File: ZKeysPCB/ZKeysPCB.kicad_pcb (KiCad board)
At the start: 2 copper layers, 73.7 x 50.8 mm, 15 parts, among them SW1 SW_Push, SW2 SW_Push, SW3 SW_Push, SW4 SW_Push, SW5 SW_Push, SW6 SW_Push, U1 Teensy-LC

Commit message: updated PCB drawing
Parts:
- removed the REF** at (87.6, 90.2)
- removed the REF** at (87.6, 132.1)
- removed the REF** at (153.7, 132.1)
- added REF**: MountingHole_3.2mm_M3, MountingHole:MountingHole_3.2mm_M3, F.Cu at (69.8, 127.0)
- added REF**: MountingHole_3.2mm_M3, MountingHole:MountingHole_3.2mm_M3, F.Cu at (69.8, 94.0)
- added REF**: MountingHole_3.2mm_M3, MountingHole:MountingHole_3.2mm_M3, F.Cu at (153.0, 127.0)
- U1: moved to F.Cu
- moved R2 68.9 mm to (68.6, 109.9), turned to 90 degrees
- moved KEY 59.4 mm to (71.8, 119.4)
- moved PWR 43.2 mm to (71.8, 114.3), turned to 180 degrees
- moved R1 42.1 mm to (71.8, 109.9), turned to 90 degrees
- moved U1 4.58 mm to (82.5, 106.7)
- moved REF** 3.24 mm to (153.0, 93.3)
- moved SW4 2.84 mm to (104.1, 115.6)
- moved SW1 2.54 mm to (104.1, 95.2)
- moved SW5 1.80 mm to (124.5, 115.6)
- moved SW6 1.27 mm to (144.8, 115.6)
- moved SW2 1.27 mm to (124.5, 95.2)
- renumbered D2 to KEY, D1 to PWR
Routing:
- net BTN_INC: track 49.4 -> 90.5 mm
- net BTN_DEC: track 28.2 -> 56.0 mm
- net Net-(D1-Pad2): track 42.5 -> 16.0 mm
- net GND: track 25.6 -> 0.00 mm
- net Net-(D2-Pad2): track 33.3 -> 8.04 mm
- net BTN_MUTE: track 10.7 -> 35.5 mm
- net Net-(D2-Pad1): track 3.81 -> 13.8 mm
- net BTN_NEXT: track 67.1 -> 74.1 mm
- net BTN_PLAY: track 47.3 -> 51.1 mm
- net BTN_PREV: track 29.0 -> 30.3 mm
- net Net-(D1-Pad1): track 3.81 -> 4.44 mm
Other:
- board size 73.7 x 50.8 mm -> 92.1 x 42.5 mm

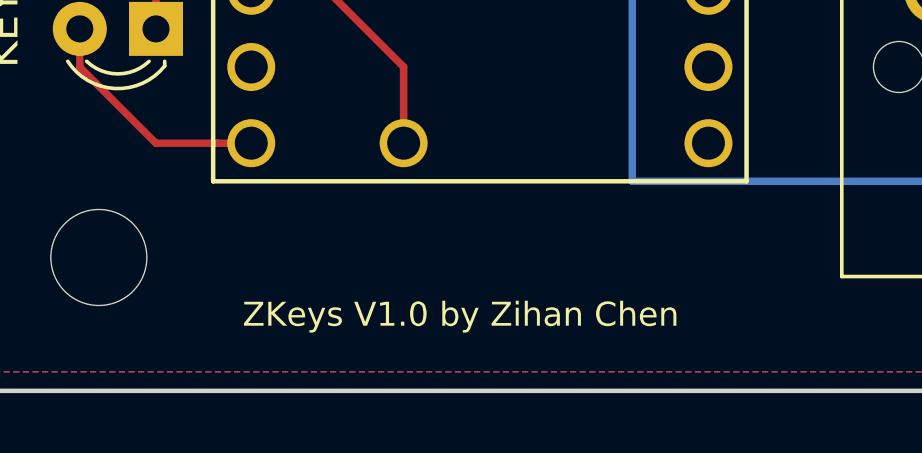
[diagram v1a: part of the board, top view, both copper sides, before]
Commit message: Added icon pretty file
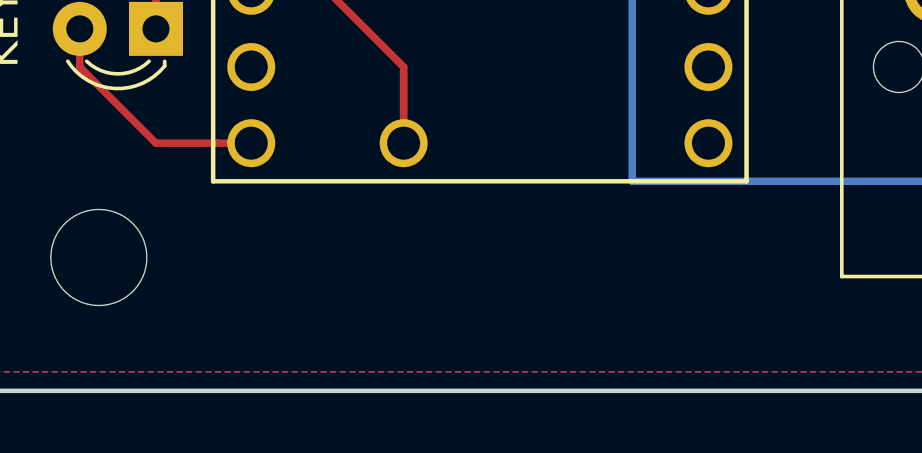
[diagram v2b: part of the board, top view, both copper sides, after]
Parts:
- added G***: LOGO, icon:icon, B.Cu at (132.1, 109.2)
